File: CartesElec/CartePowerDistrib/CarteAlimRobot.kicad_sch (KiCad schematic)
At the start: 15 parts, among them J1 Screw_Terminal_01x02, J10 Conn_01x04_Male, J2 Screw_Terminal_01x02, J3 Screw_Terminal_01x02, J4 Screw_Terminal_01x02, J5 Screw_Terminal_01x02, J6 Screw_Terminal_01x02, J7 Screw_Terminal_01x02, J8 Screw_Terminal_01x02, J9 Conn_01x03_Male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

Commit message: Carte Alim V2
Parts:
- removed J10: Conn_01x04_Male, Connector_JST:JST_XH_B4B-XH-AM_1x04_P2.50mm_Vertical, symbol Connector:Conn_01x04_Male
- removed J8: Screw_Terminal_01x02, TerminalBlock:TerminalBlock_bornier-2_P5.08mm, symbol Connector:Screw_Terminal_01x02
- removed Q1: IRF540N, Package_TO_SOT_THT:TO-220-3_Vertical, symbol Transistor_FET:IRF540N
- added J10: Conn_01x02_Male, Connector_JST:JST_EH_B2B-EH-A_1x02_P2.50mm_Vertical, symbol Connector:Conn_01x02_Male
- added J8: USB_A, Connector_USB:USB_A_Molex_67643_Horizontal, symbol Connector:USB_A
- added R3, R4, R5: R, Resistor_SMD:R_0805_2012Metric, symbol Device:R
- added U2: ASSR-1218, Package_SO:SO-4_4.4x3.6mm_P2.54mm, symbol Relay_SolidState:ASSR-1218
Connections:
- net GND_P is gone; now on net GND: J3.2 (Pin_2), J4.2 (Pin_2), J5.2 (Pin_2), J6.2 (Pin_2), J7.2 (Pin_2)
- net +12V: now also J1.2 (Pin_2); no longer J3.1 (Pin_1), J4.1 (Pin_1), J5.1 (Pin_1), J6.1 (Pin_1), J7.1 (Pin_1)
- net +5V: now also J8.1 (VBUS)
- net GND: now also J10.2 (Pin_2), J8.4 (GND), R3.1, R4.1, U2.2; no longer J1.2 (Pin_2)
- net SignalPowerOn: now also J10.1 (Pin_1), R5.1
- net at J1.1 (Pin_1): now also U2.3
- net at J9.3 (Pin_3), R1.1: now also R3.2
- new net: R4.2, R5.2, U2.1
- new net 12V_P: J3.1 (Pin_1), J4.1 (Pin_1), J5.1 (Pin_1), J6.1 (Pin_1), J7.1 (Pin_1), U2.4
- no-connect marks 0 -> 3
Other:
- note removed: "Connecteur Arrêt Urgence"

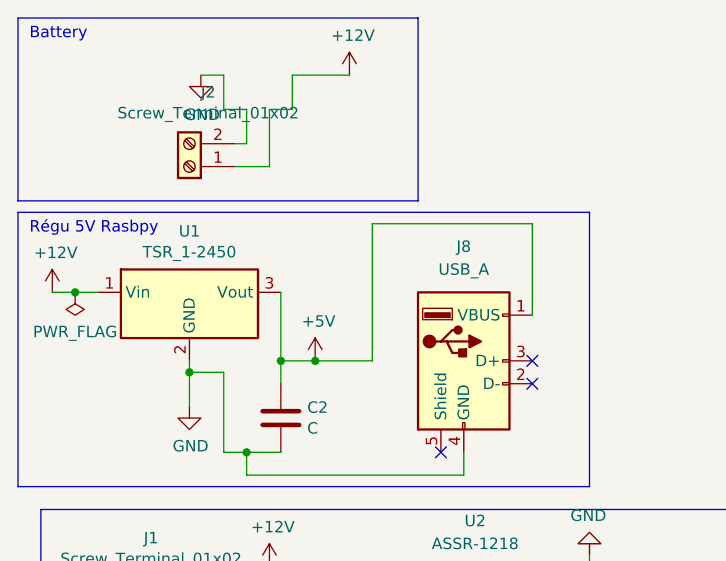
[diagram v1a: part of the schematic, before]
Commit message: Carte Alim V2.1\nAjout d'un interrupteur pour la RaspbPi
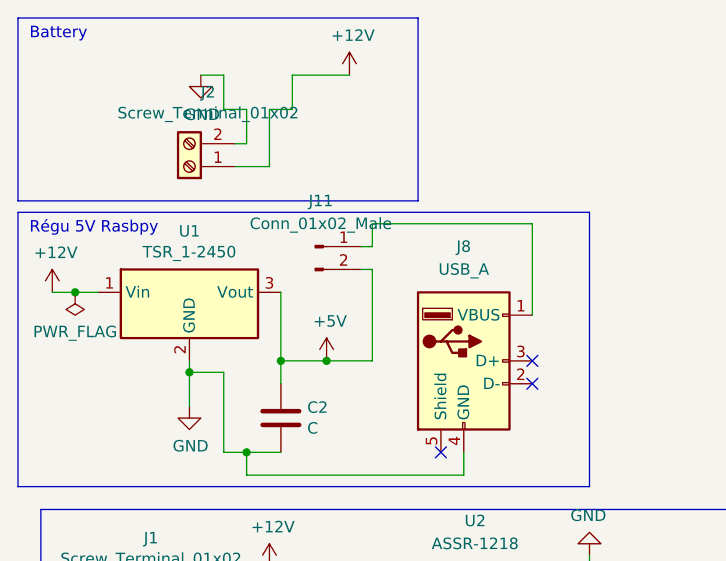
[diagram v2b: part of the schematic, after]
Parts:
- added J11: Conn_01x02_Male, Connector_JST:JST_EH_B2B-EH-A_1x02_P2.50mm_Vertical, symbol Connector:Conn_01x02_Male
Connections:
- net +5V: now also J11.2 (Pin_2); no longer J8.1 (VBUS)
- new net: J11.1 (Pin_1), J8.1 (VBUS)
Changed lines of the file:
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@@
   (junction (at 41.91 76.2) (diameter 0) (color 0 0 0 0)
   )
+  (junction (at 48.26 50.8) (diameter 0) (color 0 0 0 0)
+  )
   (junction (at 39.37 60.96) (diameter 0) (color 0 0 0 0)
   )
@@
   )
   (junction (at 77.47 74.93) (diameter 0) (color 0 0 0 0)
-  )
-  (junction (at 46.99 50.8) (diameter 0) (color 0 0 0 0)
   )
   (junction (at 43.18 50.8) (diameter 0) (color 0 0 0 0)
@@
     (stroke (width 0) (type default) (color 0 0 0 0))
   )
-  (wire (pts (xy 46.99 50.8) (xy 43.18 50.8))
+  (wire (pts (xy 53.34 38.1) (xy 53.34 35.56))
     (stroke (width 0) (type default) (color 0 0 0 0))
   )
@@
     (stroke (width 0) (type default) (color 0 0 0 0))
   )
-  (wire (pts (xy 53.34 50.8) (xy 46.99 50.8))
+  (wire (pts (xy 43.18 50.8) (xy 48.26 50.8))
     (stroke (width 0) (type default) (color 0 0 0 0))
   )
@@
     (stroke (width 0) (type default) (color 0 0 0 0))
   )
+  (wire (pts (xy 48.26 50.8) (xy 53.34 50.8))
+    (stroke (width 0) (type default) (color 0 0 0 0))
+  )
   (wire (pts (xy 53.34 35.56) (xy 71.12 35.56))
     (stroke (width 0) (type default) (color 0 0 0 0))
@@
     (stroke (width 0) (type default) (color 0 0 0 0))
   )
+  (wire (pts (xy 53.34 40.64) (xy 53.34 50.8))
+    (stroke (width 0) (type default) (color 0 0 0 0))
+  )
   (wire (pts (xy 33.02 55.88) (xy 33.02 52.07))
     (stroke (width 0) (type default) (color 0 0 0 0))
@@
     (stroke (width 0) (type default) (color 0 0 0 0))
   )
+  (wire (pts (xy 52.07 40.64) (xy 53.34 40.64))
+    (stroke (width 0) (type default) (color 0 0 0 0))
+  )
   (wire (pts (xy 36.83 52.07) (xy 33.02 52.07))
     (stroke (width 0) (type default) (color 0 0 0 0))
@@
     (stroke (width 0) (type default) (color 0 0 0 0))
   )
-  (wire (pts (xy 53.34 50.8) (xy 53.34 35.56))
+  (wire (pts (xy 52.07 38.1) (xy 53.34 38.1))
     (stroke (width 0) (type default) (color 0 0 0 0))
   )
@@
     (pin "1")
   )
-  (symbol (lib_id "power:+5V") (at 46.99 50.8 0) (unit 1)
-    (in_bom yes) (on_board yes)
-    (property "Reference" "#PWR011" (id 0) (at 46.99 54.61 0)
-      (effects (font (size 1.27 1.27)) hide)
-    )
-    (property "Value" "+5V" (id 1) (at 47.371 46.4058 0))
-    (property "Footprint" "" (id 2) (at 46.99 50.8 0)
-      (effects (font (size 1.27 1.27)) hide)
-    )
-    (property "Datasheet" "" (id 3) (at 46.99 50.8 0)
-      (effects (font (size 1.27 1.27)) hide)
-    )
-    (pin "1")
-  )
   (symbol (lib_id "power:+12V") (at 17.78 43.18 0) (unit 1)
     (in_bom yes) (on_board yes)
@@
     )
     (property "Datasheet" "~" (id 3) (at 41.91 77.47 0)
+      (effects (font (size 1.27 1.27)) hide)
+    )
+    (pin "1")
+  )
+  (symbol (lib_id "power:+5V") (at 48.26 50.8 0) (unit 1)
+    (in_bom yes) (on_board yes)
+    (property "Reference" "#PWR?" (id 0) (at 48.26 54.61 0)
+      (effects (font (size 1.27 1.27)) hide)
+    )
+    (property "Value" "+5V" (id 1) (at 48.641 46.4058 0))
+    (property "Footprint" "" (id 2) (at 48.26 50.8 0)
+      (effects (font (size 1.27 1.27)) hide)
+    )
+    (property "Datasheet" "" (id 3) (at 48.26 50.8 0)
       (effects (font (size 1.27 1.27)) hide)
     )
@@
     (pin "1")
   )
+  (symbol (lib_id "Connector:Conn_01x02_Male") (at 46.99 38.1 0) (unit 1)
+    (in_bom yes) (on_board yes) (fields_autoplaced)
+    (property "Reference" "J11" (id 0) (at 47.625 33.02 0))
+    (property "Value" "Conn_01x02_Male" (id 1) (at 47.625 35.56 0))
+    (property "Footprint" "Connector_JST:JST_EH_B2B-EH-A_1x02_P2.50mm_Vertical" (id 2) (at 46.99 38.1 0)
+      (effects (font (size 1.27 1.27)) hide)
+    )
+    (property "Datasheet" "~" (id 3) (at 46.99 38.1 0)
+      (effects (font (size 1.27 1.27)) hide)
+    )
+    (pin "1")
+    (pin "2")
+  )
   (symbol (lib_id "power:GND") (at 25.4 140.97 0) (unit 1)
     (in_bom yes) (on_board yes)
@@
       (reference "#PWR010") (unit 1) (value "GND") (footprint "")
     )
-    (path "/00000000-0000-0000-0000-000061739a43"
-      (reference "#PWR011") (unit 1) (value "+5V") (footprint "")
-    )
     (path "/00000000-0000-0000-0000-00006172f159"
       (reference "#PWR012") (unit 1) (value "+12V") (footprint "")
@@
       (reference "#PWR0101") (unit 1) (value "GND") (footprint "")
     )
+    (path "/13c8987e-255a-47c8-898a-6966f6344663"
+      (reference "#PWR?") (unit 1) (value "+5V") (footprint "")
+    )
     (path "/00000000-0000-0000-0000-00006173aca5"
       (reference "C2") (unit 1) (value "C") (footprint "Capacitor_SMD:C_0805_2012Metric")
@@
       (reference "J10") (unit 1) (value "Conn_01x02_Male") (footprint "Connector_JST:JST_EH_B2B-EH-A_1x02_P2.50mm_Vertical")
     )
+    (path "/77997343-80cf-4172-95cd-66c6bae4b1e6"
+      (reference "J11") (unit 1) (value "Conn_01x02_Male") (footprint "Connector_JST:JST_EH_B2B-EH-A_1x02_P2.50mm_Vertical")
+    )
     (path "/00000000-0000-0000-0000-00006177cc7d"
